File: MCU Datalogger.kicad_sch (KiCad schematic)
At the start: 0 parts

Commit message: schema page settings
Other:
- company: (none) -> ${name}
- title: (none) -> ${project_name}
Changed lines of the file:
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@@
 	(generator_version "9.0")
 	(paper "A4")
+	(title_block
+		(title "${project_name}")
+		(date "2025-12-21")
+		(rev "1")
+		(company "${name}")
+	)
 	(sheet_instances
 		(path "/"

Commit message: Add schem symbols'
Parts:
- added BT1: Battery, symbol Device:Battery
- added C1, C2, C3, C4: C, symbol Device:C
- added C5: C_Polarized, symbol Device:C_Polarized
- added D1, D2: LED, SparkFun-LED:LED_0603_1608Metric, symbol SparkFun-LED:LED
- added H1, H2, H3, H4: MountingHole, symbol Mechanical:MountingHole
- added R1, R2, R3, R4, R5, R6, R7: R, symbol Device:R
- added U1, U2: 24LC1025, symbol Memory_EEPROM:24LC1025
- added U3: ATMEGA328P-AU, ATMEGA328P-AU:QFP80P900X900X120-32N, symbol ATMEGA328P-AU:ATMEGA328P-AU
- added U4: DS1337S_, DS1337S_:SOIC127P600X175-8N, symbol DS1337S_:DS1337S_
- added Y1, Y2: Crystal, symbol Device:Crystal
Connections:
- new net GND: U3.21 (GND), U3.3 (GND), U3.5 (GND)
- new net VCC: U3.4 (VCC), U3.6 (VCC)
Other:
- added sheet Connectors (connectors.kicad_sch)

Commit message: finish schema design
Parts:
- BT1: footprint (none) -> Connector_PinHeader_2.54mm:PinHeader_2x01_P2.54mm_Vertical_SMD
- C1, C4: value C -> 0.1uF; footprint (none) -> Capacitor_SMD:C_0805_2012Metric
- C2: renamed from C3; value C -> 22pF; footprint (none) -> Capacitor_SMD:C_0805_2012Metric
- C3: renamed from C2; value C -> 22pF; footprint (none) -> Capacitor_SMD:C_0805_2012Metric
- C5: value C_Polarized -> 100nF; footprint (none) -> Capacitor_SMD:C_0805_2012Metric
- D1, D2: footprint SparkFun-LED:LED_0603_1608Metric -> LED_SMD:LED_0805_2012Metric; symbol SparkFun-LED:LED -> Device:LED
- H1, H2, H3, H4: footprint (none) -> MountingHole:MountingHole_2.1mm
- R1: renamed from R3; value R -> 10K; footprint (none) -> Resistor_SMD:R_0805_2012Metric
- R2: renamed from R4; value R -> 10K; footprint (none) -> Resistor_SMD:R_0805_2012Metric
- R3: renamed from R1; value R -> 4.7K; footprint (none) -> Resistor_SMD:R_0805_2012Metric
- R4: renamed from R2; value R -> 4.7K; footprint (none) -> Resistor_SMD:R_0805_2012Metric
- R5: renamed from R7; value R -> 330; footprint (none) -> Resistor_SMD:R_0805_2012Metric
- R6: value R -> 10K; footprint (none) -> Resistor_SMD:R_0805_2012Metric
- R7: renamed from R5; value R -> 330; footprint (none) -> Resistor_SMD:R_0805_2012Metric
- U2: renamed from U1; footprint (none) -> Package_SO:SOIC-8_5.3x5.3mm_P1.27mm
- U3: renamed from U2; footprint (none) -> Package_SO:SOIC-8_5.3x5.3mm_P1.27mm
- Y1: renamed from Y2; value Crystal -> 32.768 KHz; footprint (none) -> Crystal:Crystal_SMD_5032-2Pin_5.0x3.2mm_HandSoldering
- Y2: renamed from Y1; value Crystal -> 16 MHz; footprint (none) -> Crystal:Crystal_SMD_5032-2Pin_5.0x3.2mm_HandSoldering
- renumbered U4 to U1, U3 to U4
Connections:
- net GND: now also BT1.2 (-), C1.2, C2.1, C3.1, C4.1, C5.2, R5.1, R7.2, U1.4 (GND), U2.4 (GND), U2.7 (WP), U3.2 (A1), U3.4 (GND), U3.7 (WP)
- net VCC: now also C1.1, R1.1, R2.1, R3.1, R4.1, R6.1, U1.8 (VCC), U2.1 (A0), U2.2 (A1), U2.3 (A2), U2.8 (VCC), U3.1 (A0), U3.3 (A2), U3.8 (VCC); no longer U4.4 (VCC), U4.6 (VCC)
- net RESET: now reaches R6.2
- net RESET: now also U4.29 (PC6/~{RESET})
- net at C3.2: now also U4.8 (PB7), Y2.1
- net at D2.1 (K): now also R7.1
- net at D2.2 (A): now also BT1.1 (+), C5.1, U4.18 (AVCC), U4.4 (VCC)
- net at C2.2: now also U4.7 (PB6), Y2.2
- net SDA: now reaches U2.5 (SDA)
- net SDA: now also R4.2, U1.5 (SDA), U3.5 (SDA), U4.27 (PC4)
- net SCK: now reaches U2.6 (SCL)
- net SCK: now also D1.2 (A), R3.2, U1.6 (SCL), U3.6 (SCL), U4.17 (PB5), U4.28 (PC5)
- net at R1.2: now also U1.3 (~{INTA})
- net at Y1.1: now also U1.2 (X2)
- net at Y1.2: now also U1.1 (X1)
- net at R2.2: now also U1.7 (SQW/~INT)
- net at R5.2: now also D1.1 (K)
- net D3: now reaches U4.1 (PD3)
- net D6: now reaches U4.10 (PD6)
- net D7: now reaches U4.11 (PD7)
- net D8: now reaches U4.12 (PB0)
- net MOSI: now reaches U4.15 (PB3)
- net MISO: now reaches U4.16 (PB4)
- net D4: now reaches U4.2 (PD4)
- net at U4.20 (AREF): now also C4.2
- net RX: now reaches U4.30 (PD0)
- net TX: now reaches U4.31 (PD1)
- net D2: now reaches U4.32 (PD2)
- net D5: now reaches U4.9 (PD5)
- no-connect marks 0 -> 9
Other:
- sheet Connectors ports: added D2, D3, D4, D5, D6, D7, D8, GND, MISO, MOSI, RESET, RX, SCK, SDA, TX, VCC; removed none
- moved on the sheet: BT1, C1, C2, C3, C4, C5, D1, D2, H1, H2, H3, H4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

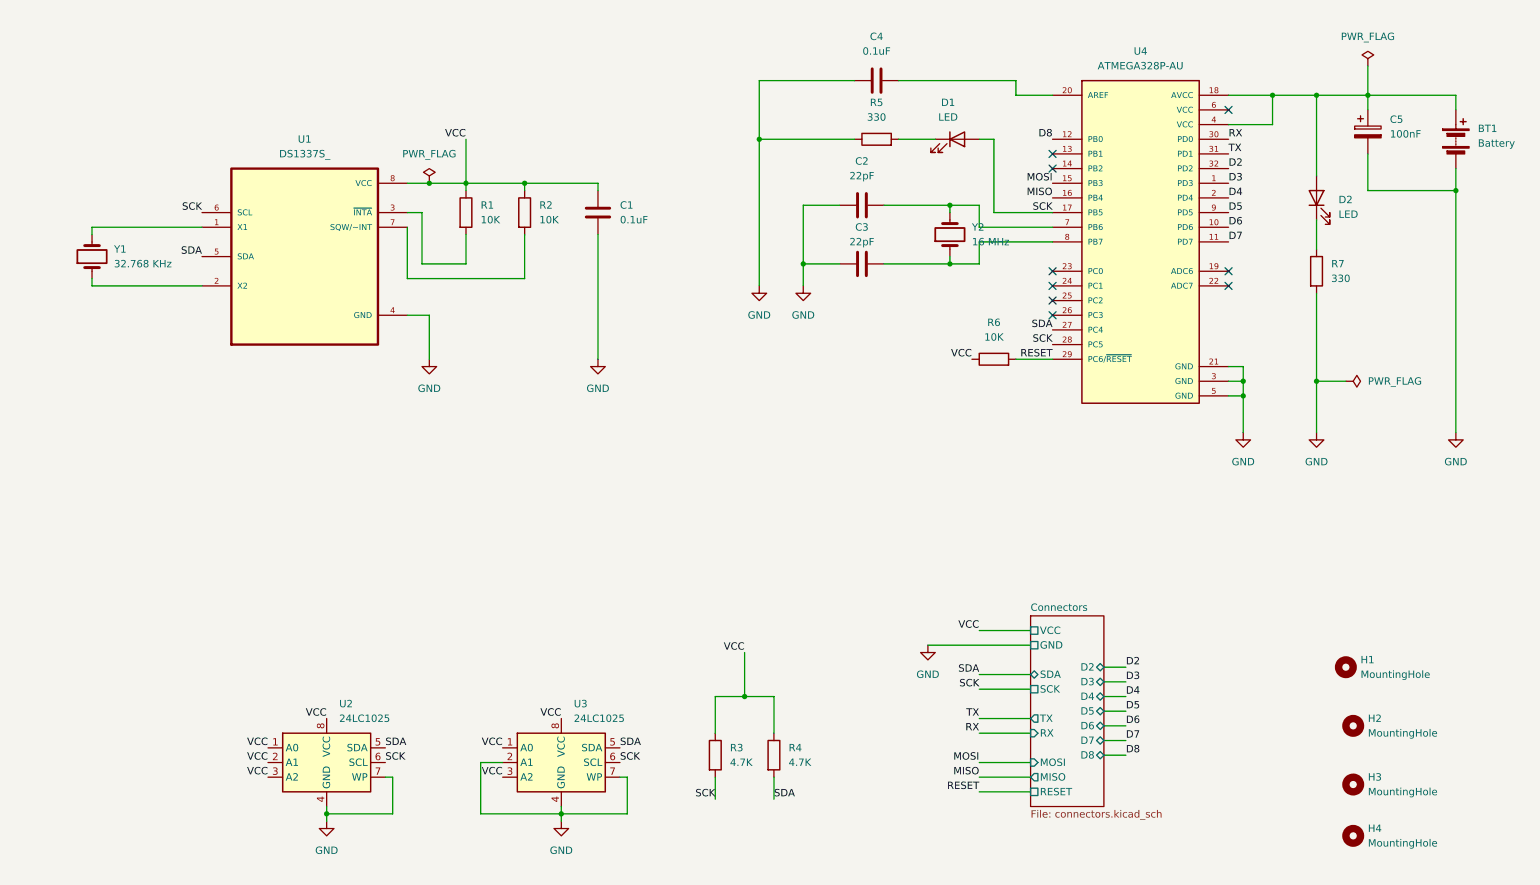
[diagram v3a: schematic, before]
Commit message: update conn_02x03 footprint
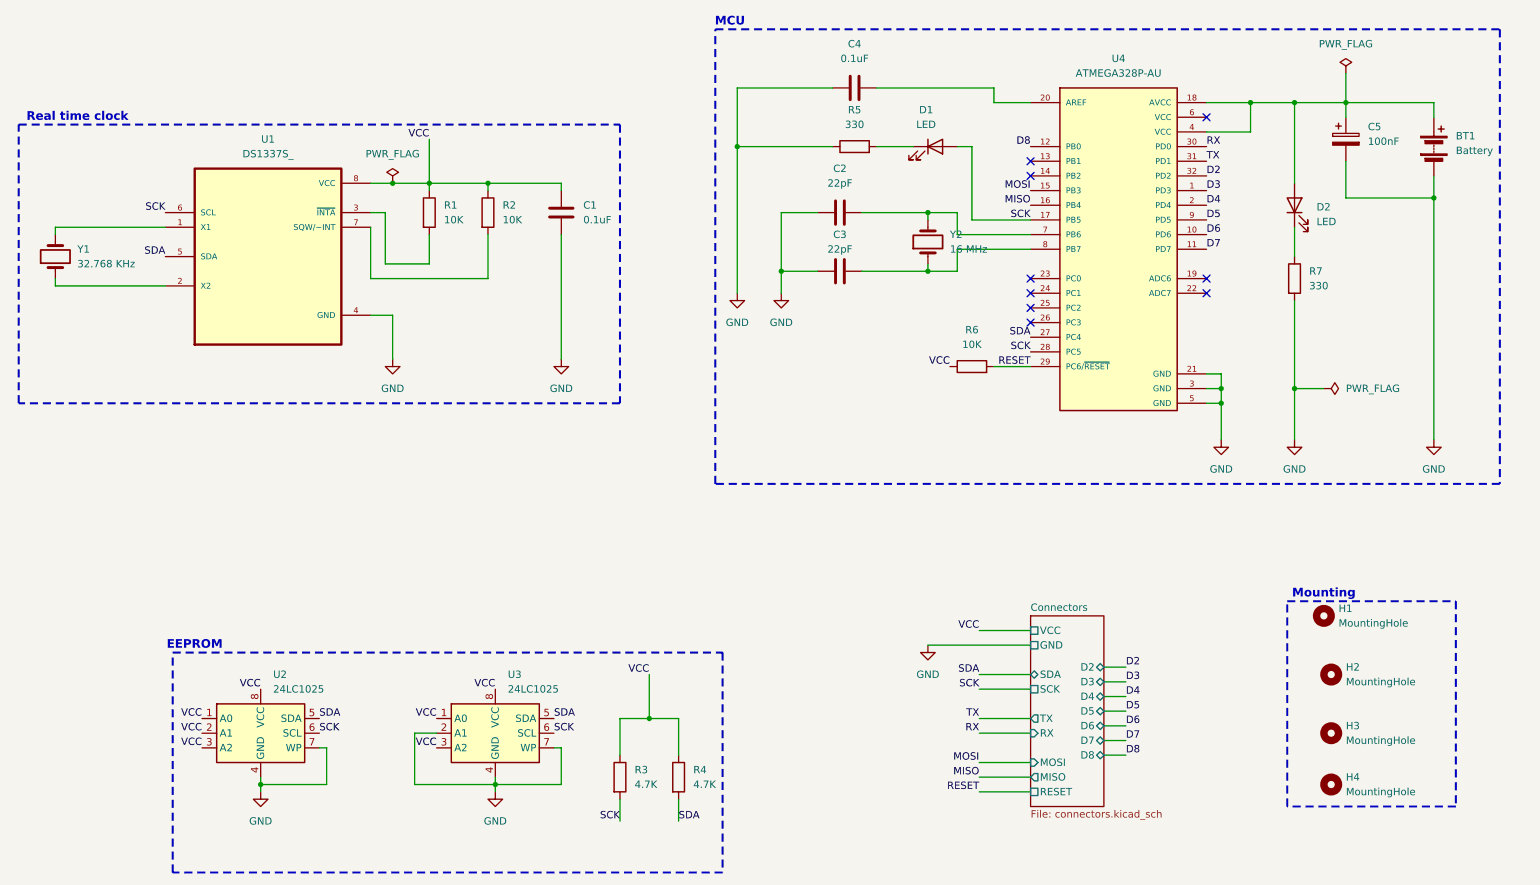
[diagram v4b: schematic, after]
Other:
- note added: "EEPROM"
- note added: "MCU"
- note added: "Mounting"
- note added: "Real time clock"
- moved on the sheet: BT1, C1, C2, C3, C4, C5, D1, D2, H1, H2, H3, H4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

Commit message: finish routing
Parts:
- BT1: footprint Connector_PinHeader_2.54mm:PinHeader_2x01_P2.54mm_Vertical_SMD -> Connector_PinHeader_2.54mm:PinHeader_2x01_P2.54mm_Vertical
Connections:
- net VCC: now also BT1.1 (+), C5.1, D2.2 (A), U4.18 (AVCC), U4.4 (VCC)
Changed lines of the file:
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@@
+	)
+	(label "VCC"
+		(at 264.16 31.75 180)
+		(effects
+			(font
+				(size 1.27 1.27)
+			)
+			(justify right bottom)
+		)
 	)
 	(label "VCC"
@@
 			)
 		)
-		(property "Footprint" "Connector_PinHeader_2.54mm:PinHeader_2x01_P2.54mm_Vertical_SMD"
+		(property "Footprint" "Connector_PinHeader_2.54mm:PinHeader_2x01_P2.54mm_Vertical"
 			(at 269.24 37.846 90)
 			(effects
